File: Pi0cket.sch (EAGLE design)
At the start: 13 parts, among them T1 SI2301, U1 Tiny85-20-SMT

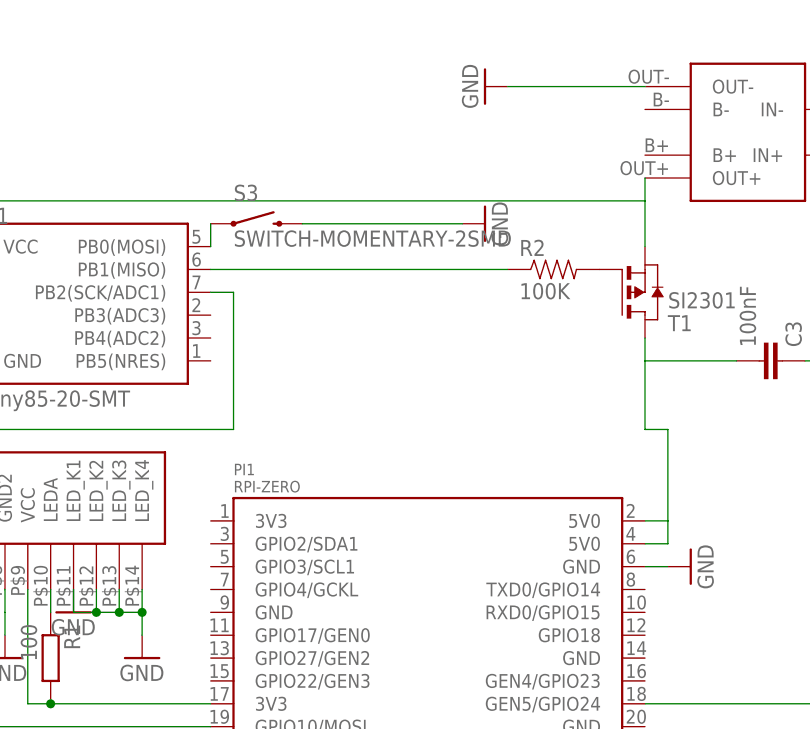
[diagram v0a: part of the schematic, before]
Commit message: some tweaks
added i2c lines from the attiny to the pi (might live to regret that!!)

re-arranged the tiny and associated bits to make things flow better

added battery socket back in for ease of external charging

moved backlight resistor to save some space
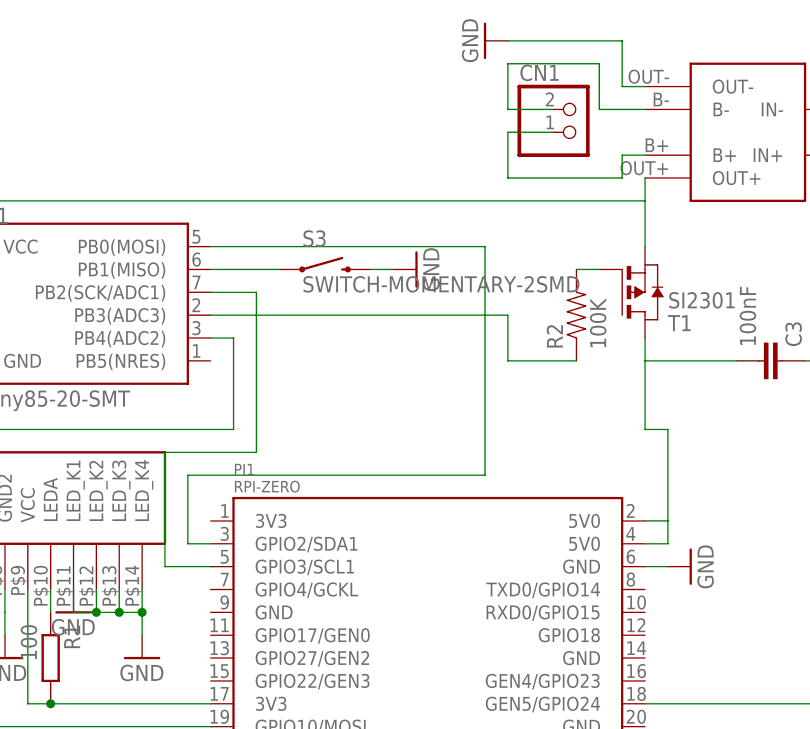
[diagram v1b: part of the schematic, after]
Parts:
- added CN1: (no value), adafruit:JST_2PIN-SMT-RA
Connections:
- new net N$16: S3.1, U1.PB1(MISO)
- new net N$20: R2.1, U1.PB3(ADC3)
- new net N$26: D1.DIN, U1.PB4(ADC2)
- new net N$29: CN1.1, POWER1.B-
- net N$24: now also CN1.2, POWER1.B+; no longer R2.1, U1.PB1(MISO)
- net N$25: now also PI1.GPIO2/SDA1; no longer S3.1
- net N$28: now also PI1.GPIO3/SCL1; no longer D1.DIN
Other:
- moved on the sheet: R2, S3
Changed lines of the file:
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@@
 <part name="GND9" library="supply1" deviceset="GND" device=""/>
 <part name="D1" library="SparkFun-LED" deviceset="WS2812B" device=""/>
+<part name="CN1" library="adafruit" deviceset="JST_2PIN" device="-SMT-RA"/>
 </parts>
 <sheets>
@@
 <instance part="SCREEN1" gate="G$1" x="-45.72" y="83.82" rot="R90"/>
 <instance part="PI1" gate="G$1" x="0" y="50.8"/>
-<instance part="GND1" gate="1" x="7.62" y="129.54" rot="R270"/>
+<instance part="GND1" gate="1" x="7.62" y="134.62" rot="R270"/>
 <instance part="POWER1" gate="G$1" x="38.1" y="124.46" rot="R180"/>
 <instance part="GND4" gate="1" x="-45.72" y="66.04"/>
@@
 <instance part="GND6" gate="1" x="-55.88" y="96.52"/>
 <instance part="T1" gate="A" x="25.4" y="106.68" rot="MR180"/>
-<instance part="R2" gate="G$1" x="15.24" y="109.22"/>
+<instance part="R2" gate="G$1" x="17.78" y="104.14" rot="R90"/>
 <instance part="C3" gate="G$1" x="40.64" y="99.06" rot="MR90"/>
 <instance part="GND7" gate="1" x="-38.1" y="71.12"/>
 <instance part="C1" gate="G$1" x="-55.88" y="106.68"/>
 <instance part="GND8" gate="1" x="48.26" y="99.06" rot="R90"/>
-<instance part="S3" gate="G$1" x="-17.78" y="114.3"/>
-<instance part="GND9" gate="1" x="7.62" y="114.3" rot="R90"/>
+<instance part="S3" gate="G$1" x="-10.16" y="109.22"/>
+<instance part="GND9" gate="1" x="0" y="109.22" rot="R90"/>
 <instance part="D1" gate="G$1" x="-66.04" y="106.68" rot="MR0"/>
+<instance part="CN1" gate="G$1" x="17.78" y="124.46"/>
 </instances>
 <busses>
@@
 <pinref part="PI1" gate="G$1" pin="GND@8"/>
 <wire x1="27.94" y1="76.2" x2="25.4" y2="76.2" width="0.1524" layer="91"/>
-</segment>
-<segment>
-<pinref part="POWER1" gate="G$1" pin="OUT-"/>
-<wire x1="25.4" y1="129.54" x2="10.16" y2="129.54" width="0.1524" layer="91"/>
-<pinref part="GND1" gate="1" pin="GND"/>
 </segment>
 <segment>
@@
 <pinref part="S3" gate="G$1" pin="2"/>
 <pinref part="GND9" gate="1" pin="GND"/>
-<wire x1="5.08" y1="114.3" x2="-12.7" y2="114.3" width="0.1524" layer="91"/>
+<wire x1="-2.54" y1="109.22" x2="-5.08" y2="109.22" width="0.1524" layer="91"/>
+</segment>
+<segment>
+<pinref part="GND1" gate="1" pin="GND"/>
+<wire x1="10.16" y1="134.62" x2="22.86" y2="134.62" width="0.1524" layer="91"/>
+<wire x1="22.86" y1="134.62" x2="22.86" y2="129.54" width="0.1524" layer="91"/>
+<wire x1="22.86" y1="129.54" x2="25.4" y2="129.54" width="0.1524" layer="91"/>
+<pinref part="POWER1" gate="G$1" pin="OUT-"/>
 </segment>
 </net>
@@
 <pinref part="T1" gate="A" pin="G"/>
 <pinref part="R2" gate="G$1" pin="2"/>
+<wire x1="17.78" y1="109.22" x2="20.32" y2="109.22" width="0.1524" layer="91"/>
 </segment>
 </net>
@@
 </segment>
 </net>
-<net name="N$24" class="0">
-<segment>
-<pinref part="U1" gate="G$1" pin="PB1(MISO)"/>
-<wire x1="-22.86" y1="109.22" x2="10.16" y2="109.22" width="0.1524" layer="91"/>
-<pinref part="R2" gate="G$1" pin="1"/>
-</segment>
-</net>
 <net name="N$25" class="0">
 <segment>
 <pinref part="U1" gate="G$1" pin="PB0(MOSI)"/>
-<pinref part="S3" gate="G$1" pin="1"/>
-<wire x1="-22.86" y1="114.3" x2="-22.86" y2="111.76" width="0.1524" layer="91"/>
+<pinref part="PI1" gate="G$1" pin="GPIO2/SDA1"/>
+<wire x1="-22.86" y1="78.74" x2="-25.4" y2="78.74" width="0.1524" layer="91"/>
+<wire x1="-25.4" y1="78.74" x2="-25.4" y2="86.36" width="0.1524" layer="91"/>
+<wire x1="-25.4" y1="86.36" x2="7.62" y2="86.36" width="0.1524" layer="91"/>
+<wire x1="7.62" y1="86.36" x2="7.62" y2="111.76" width="0.1524" layer="91"/>
+<wire x1="7.62" y1="111.76" x2="-22.86" y2="111.76" width="0.1524" layer="91"/>
 </segment>
 </net>
@@
 <segment>
 <pinref part="U1" gate="G$1" pin="PB2(SCK/ADC1)"/>
+<pinref part="PI1" gate="G$1" pin="GPIO3/SCL1"/>
+<wire x1="-22.86" y1="76.2" x2="-27.94" y2="76.2" width="0.1524" layer="91"/>
+<wire x1="-27.94" y1="76.2" x2="-27.94" y2="88.9" width="0.1524" layer="91"/>
+<wire x1="-27.94" y1="88.9" x2="-17.78" y2="88.9" width="0.1524" layer="91"/>
+<wire x1="-17.78" y1="88.9" x2="-17.78" y2="106.68" width="0.1524" layer="91"/>
+<wire x1="-17.78" y1="106.68" x2="-22.86" y2="106.68" width="0.1524" layer="91"/>
+</segment>
+</net>
+<net name="N$26" class="0">
+<segment>
 <pinref part="D1" gate="G$1" pin="DIN"/>
 <wire x1="-83.82" y1="111.76" x2="-86.36" y2="111.76" width="0.1524" layer="91"/>
 <wire x1="-86.36" y1="111.76" x2="-86.36" y2="91.44" width="0.1524" layer="91"/>
 <wire x1="-86.36" y1="91.44" x2="-20.32" y2="91.44" width="0.1524" layer="91"/>
-<wire x1="-20.32" y1="91.44" x2="-20.32" y2="106.68" width="0.1524" layer="91"/>
-<wire x1="-20.32" y1="106.68" x2="-22.86" y2="106.68" width="0.1524" layer="91"/>
-</segment>
-</net>
+<wire x1="-20.32" y1="91.44" x2="-20.32" y2="101.6" width="0.1524" layer="91"/>
+<pinref part="U1" gate="G$1" pin="PB4(ADC2)"/>
+<wire x1="-20.32" y1="101.6" x2="-22.86" y2="101.6" width="0.1524" layer="91"/>
+</segment>
+</net>
+<net name="N$16" class="0">
+<segment>
+<pinref part="S3" gate="G$1" pin="1"/>
+<pinref part="U1" gate="G$1" pin="PB1(MISO)"/>
+<wire x1="-15.24" y1="109.22" x2="-22.86" y2="109.22" width="0.1524" layer="91"/>
+</segment>
+</net>
+<net name="N$20" class="0">
+<segment>
+<pinref part="U1" gate="G$1" pin="PB3(ADC3)"/>
+<wire x1="-22.86" y1="104.14" x2="10.16" y2="104.14" width="0.1524" layer="91"/>
+<wire x1="10.16" y1="104.14" x2="10.16" y2="99.06" width="0.1524" layer="91"/>
+<pinref part="R2" gate="G$1" pin="1"/>
+<wire x1="10.16" y1="99.06" x2="17.78" y2="99.06" width="0.1524" layer="91"/>
+</segment>
+</net>
+<net name="N$24" class="0">
+<segment>
+<pinref part="POWER1" gate="G$1" pin="B+"/>
+<wire x1="25.4" y1="121.92" x2="22.86" y2="121.92" width="0.1524" layer="91"/>
+<wire x1="22.86" y1="121.92" x2="22.86" y2="119.38" width="0.1524" layer="91"/>
+<wire x1="22.86" y1="119.38" x2="10.16" y2="119.38" width="0.1524" layer="91"/>
+<wire x1="10.16" y1="119.38" x2="10.16" y2="124.46" width="0.1524" layer="91"/>
+<pinref part="CN1" gate="G$1" pin="2"/>
+<wire x1="10.16" y1="124.46" x2="15.24" y2="124.46" width="0.1524" layer="91"/>
+</segment>
+</net>
+<net name="N$29" class="0">
+<segment>
+<pinref part="CN1" gate="G$1" pin="1"/>
+<wire x1="15.24" y1="127" x2="10.16" y2="127" width="0.1524" layer="91"/>
+<wire x1="10.16" y1="127" x2="10.16" y2="132.08" width="0.1524" layer="91"/>
+<wire x1="10.16" y1="132.08" x2="20.32" y2="132.08" width="0.1524" layer="91"/>
+<wire x1="20.32" y1="132.08" x2="20.32" y2="127" width="0.1524" layer="91"/>
+<pinref part="POWER1" gate="G$1" pin="B-"/>
+<wire x1="20.32" y1="127" x2="25.4" y2="127" width="0.1524" layer="91"/>
+</segment>
+</net>
